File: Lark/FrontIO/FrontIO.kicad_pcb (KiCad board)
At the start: 2 copper layers, 86 x 14 mm, 7 parts, among them J1 0530470810, J2 0530470210, SW1 TS04-66-65-BK-100-SMT, SW2 TS04-66-65-BK-100-SMT, SW3 TS04-66-65-BK-100-SMT

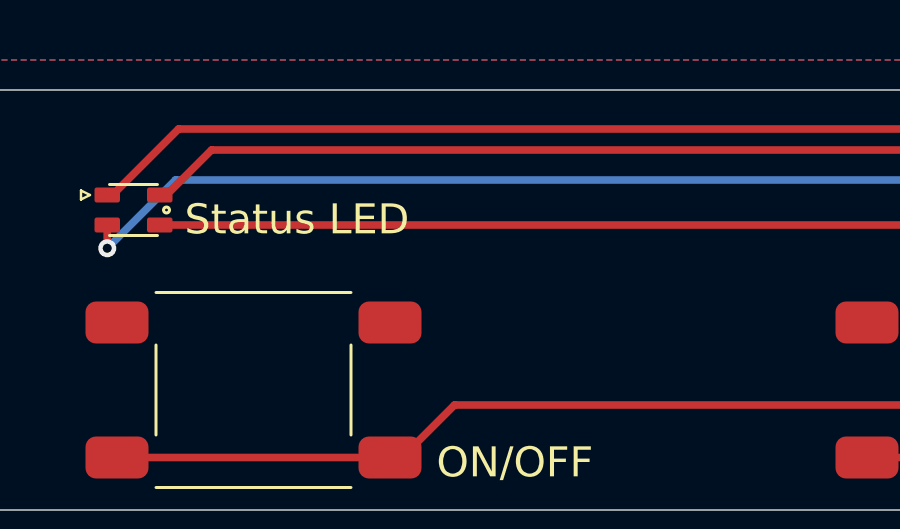
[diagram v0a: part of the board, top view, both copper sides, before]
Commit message: Created STLink Adapter PCB
- changed silk on FrontIO PCB a little.
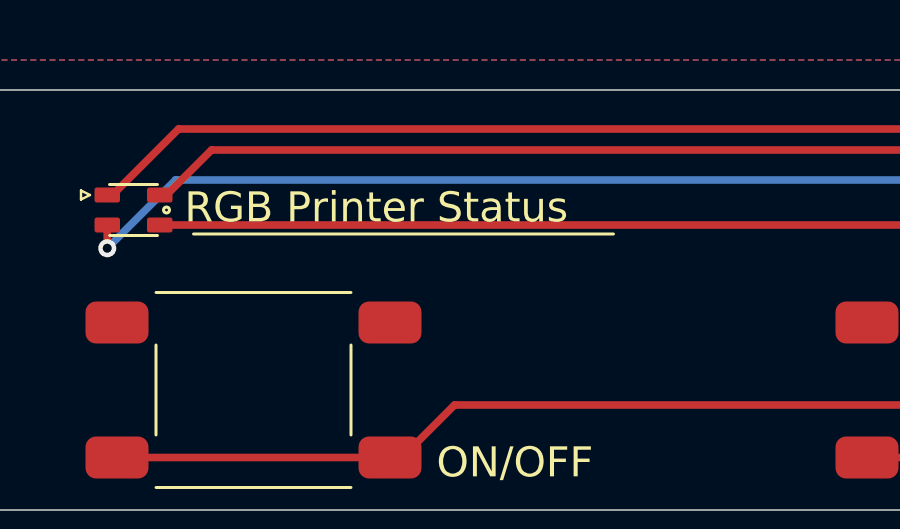
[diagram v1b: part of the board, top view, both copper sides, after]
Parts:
- added G***: LOGO, LOGO, B.Cu at (126.4, 97.2)
- moved G*** 3.50 mm to (150.4, 96.0)
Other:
- board text added: "HamSlices - 10/2025"
- board text added: "RGB Printer Status"
- board text added: "https://github.com/HamSlices"
- board text removed: "10/2025"
- board text removed: "HamSlices"
- board text removed: "Status LED"
